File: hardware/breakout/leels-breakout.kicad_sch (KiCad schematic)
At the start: 18 parts, among them J2 Servo: 5V STEP DIR ENA GND, J3 Encoder: 5V GND A B Z, J4 5V in, J5 Nextion: 5V GND TX RX, J6 Shield GND, Q1 2N3904, U1 ESP32-C6-DevKitC-1, U2 74AHCT125

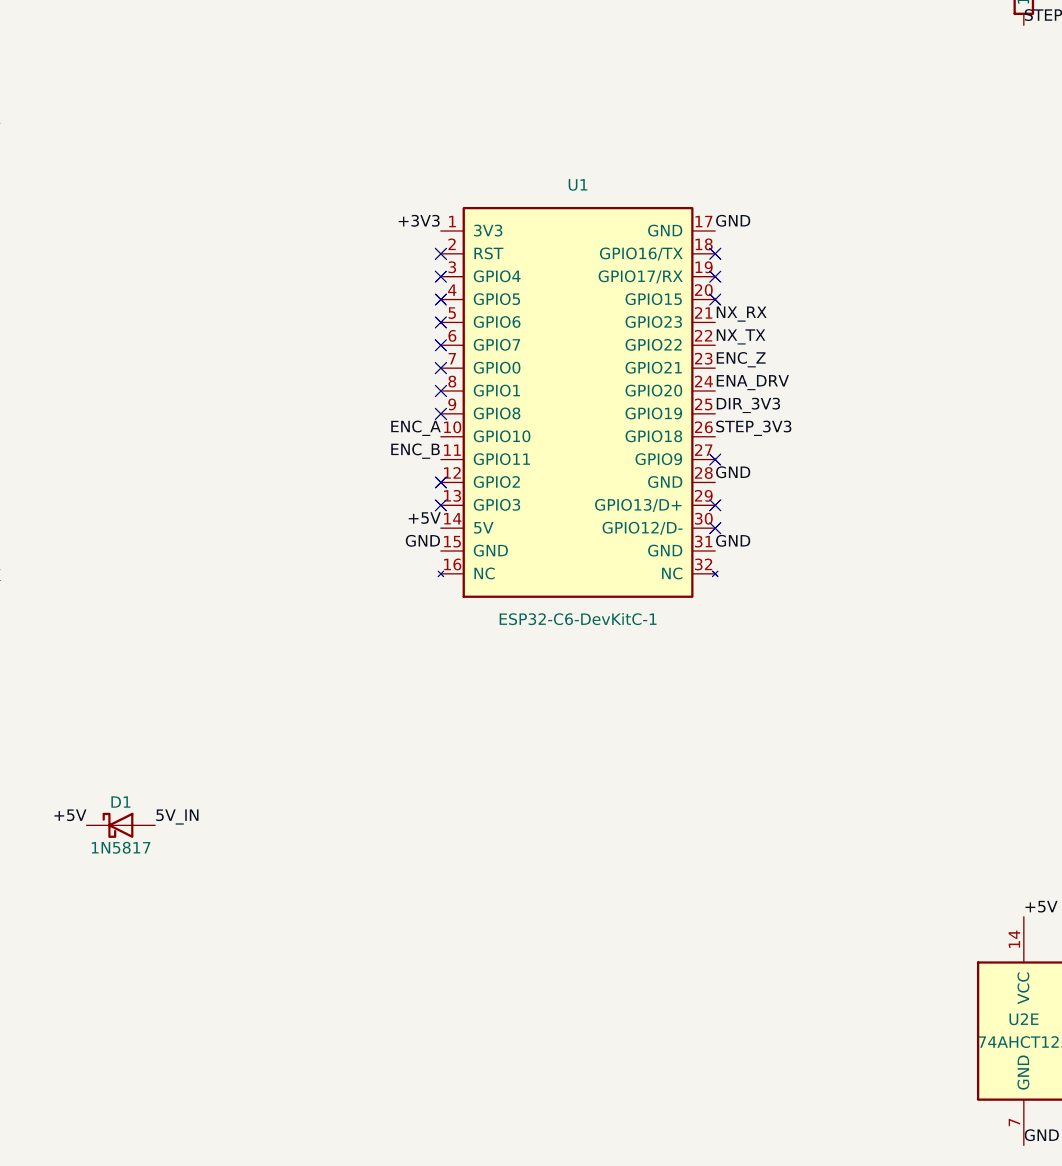
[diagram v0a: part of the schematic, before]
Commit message: Breakout: Espressif's DevKitC-1 symbol and footprint for U1
Use PCM_Espressif:ESP32-C6-DevKitC-1 (headers 22.86 mm apart, J3 pads
numbered 17-32 bottom to top) instead of the hand-made symbol, with the
nets reattached in Espressif's numbering and PWR_FLAGs on the rails.
ERC clean, no unconnected pins or orphan labels.

Co-Authored-By: Claude Opus 5.5 <noreply@anthropic.com>
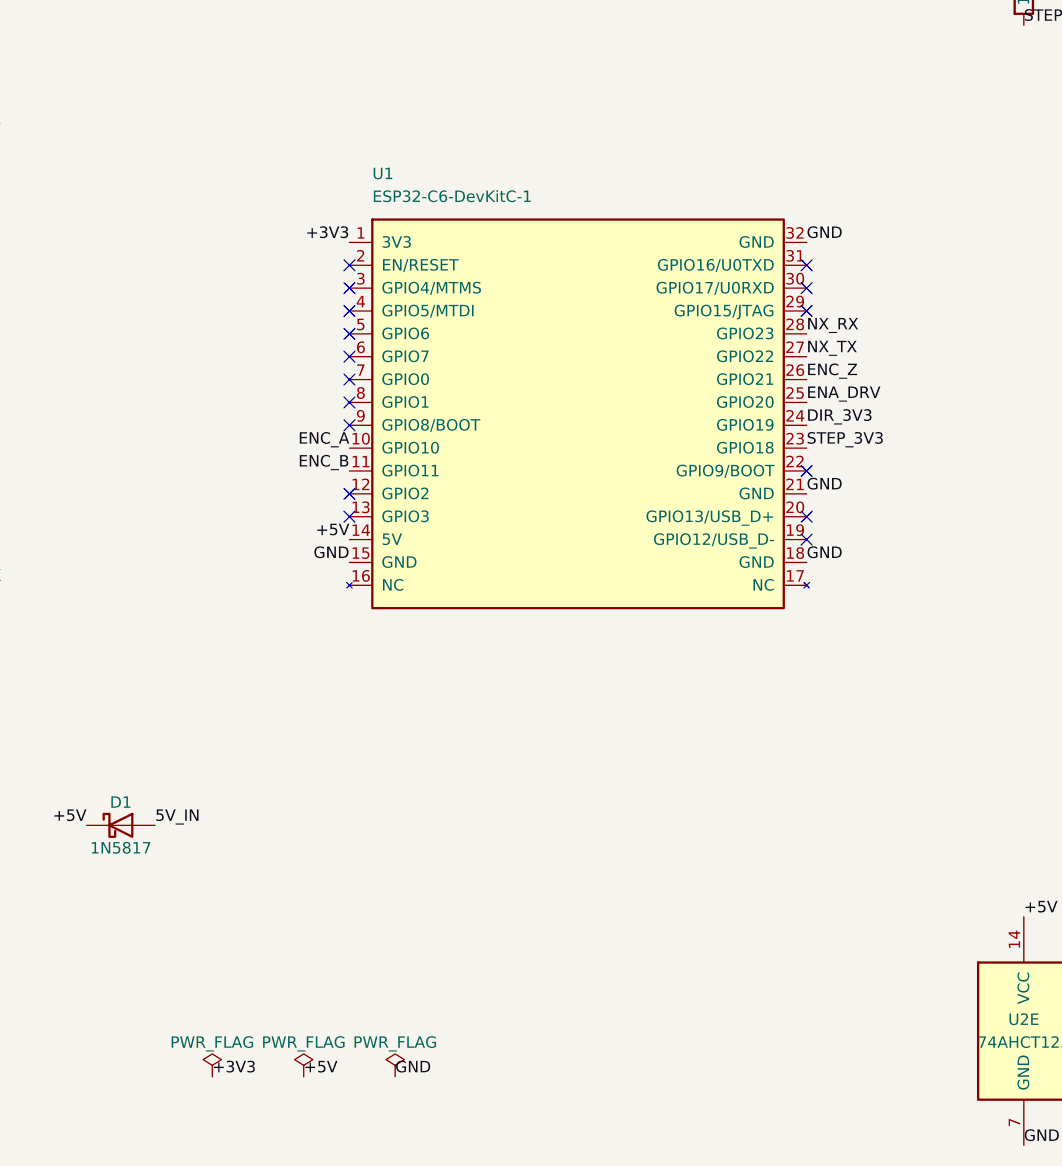
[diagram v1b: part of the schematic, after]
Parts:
- removed U1: ESP32-C6-DevKitC-1, symbol leels:ESP32-C6-DevKitC-1
- added U1: ESP32-C6-DevKitC-1, PCM_Espressif:ESP32-C6-DevKitC-1, symbol PCM_Espressif:ESP32-C6-DevKitC-1
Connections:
- net +3V3: now also U1.1 (3V3)
- net +5V: now also U1.14 (5V)
- net DIR_3V3: now also U1.24 (GPIO19)
- net ENA_DRV: now also U1.25 (GPIO20)
- net ENC_A: now also U1.10 (GPIO10)
- net ENC_B: now also U1.11 (GPIO11)
- net ENC_Z: now also U1.26 (GPIO21)
- net GND: now also U1.15 (GND), U1.18 (GND), U1.21 (GND), U1.32 (GND)
- net NX_RX: now also U1.28 (GPIO23)
- net NX_TX: now also U1.27 (GPIO22)
- net STEP_3V3: now also U1.23 (GPIO18)

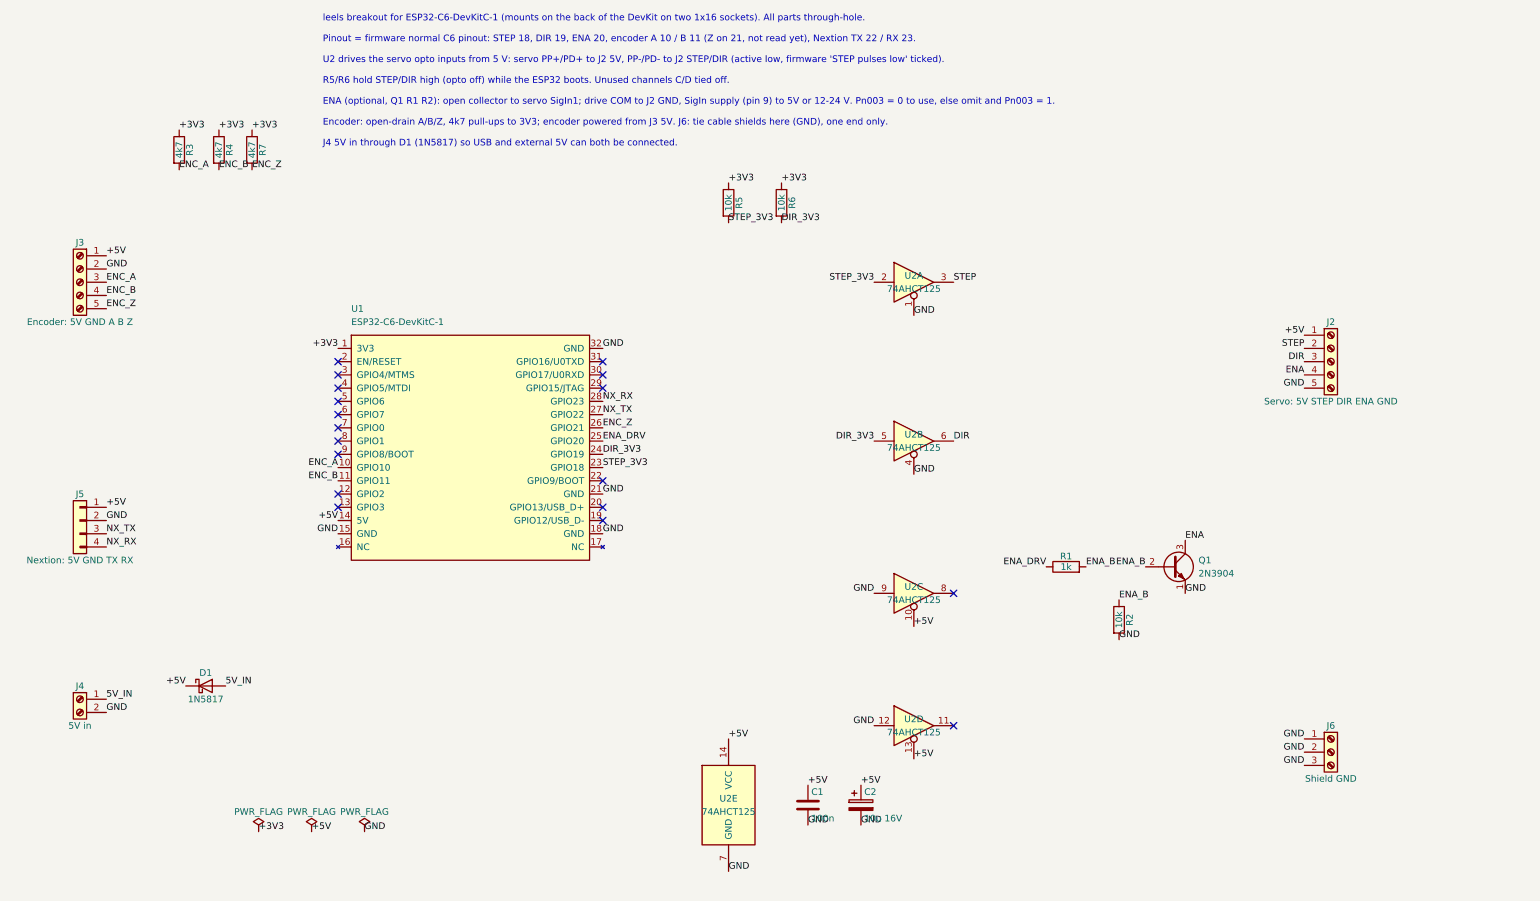
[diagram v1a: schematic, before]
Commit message: Breakout schematic: laid out by function, wired, labels only for ENC_Z
Encoder and power in on the left, the DevKit in the middle, the servo
chain (pull-ups, 74AHCT125, ENA transistor, terminal) and Nextion on the
right. Real wires and power symbols throughout; the only labels are the
ENC_Z global labels, which cross the sheet. PWR_FLAGs in their own block,
notes and title block. ERC clean, no orphans or unconnected pins.

Co-Authored-By: Claude Opus 5.5 <noreply@anthropic.com>
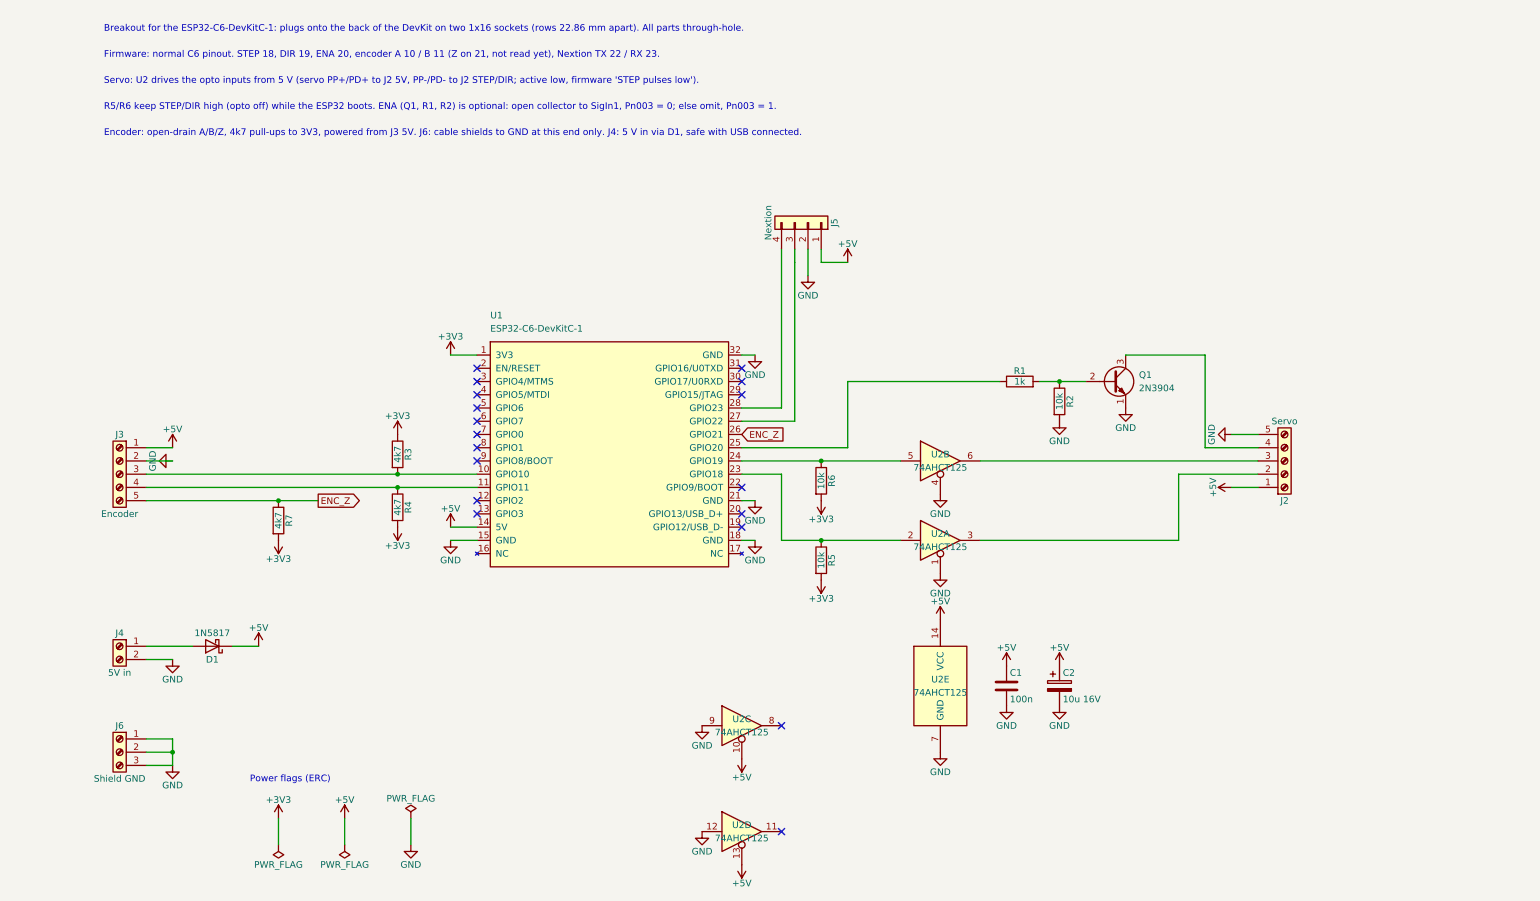
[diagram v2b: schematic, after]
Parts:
- J2: value Servo: 5V STEP DIR ENA GND -> Servo
- J3: value Encoder: 5V GND A B Z -> Encoder
- J5: value Nextion: 5V GND TX RX -> Nextion
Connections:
- net +3V3: now also R4.2, R5.2, R6.2, R7.2; no longer R4.1, R5.1, R6.1, R7.1
- net ENC_Z: now also R7.1; no longer R7.2
- net 5V_IN: no longer names the net of D1.2 (A), J4.1 (Pin_1)
- net DIR: no longer names the net of J2.3 (Pin_3), U2.6
- net DIR_3V3: no longer names the net of U1.24 (GPIO19), U2.5
- net DIR_3V3: now also R6.1; no longer R6.2
- net ENA: no longer names the net of J2.4 (Pin_4), Q1.3 (C)
- net ENA_B: no longer names the net of Q1.2 (B), R1.2, R2.1
- net ENA_DRV: no longer names the net of R1.1, U1.25 (GPIO20)
- net ENC_A: no longer names the net of J3.3 (Pin_3), R3.2, U1.10 (GPIO10)
- net ENC_B: no longer names the net of J3.4 (Pin_4), U1.11 (GPIO11)
- net ENC_B: now also R4.1; no longer R4.2
- net NX_RX: no longer names the net of J5.4 (Pin_4), U1.28 (GPIO23)
- net NX_TX: no longer names the net of J5.3 (Pin_3), U1.27 (GPIO22)
- net STEP: no longer names the net of J2.2 (Pin_2), U2.3
- net STEP_3V3: no longer names the net of U1.23 (GPIO18), U2.2
- net STEP_3V3: now also R5.1; no longer R5.2
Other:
- note added: "Breakout for the ESP32-C6-DevKitC-1: plugs onto the back of the DevKit on two 1x16 sockets (rows 22.86 mm apart). All parts through-hole."
- note added: "Encoder: open-drain A/B/Z, 4k7 pull-ups to 3V3, powered from J3 5V. J6: cable shields to GND at this end only. J4: 5 V in via D1, safe with USB connected."
- note added: "Firmware: normal C6 pinout. STEP 18, DIR 19, ENA 20, encoder A 10 / B 11 (Z on 21, not read yet), Nextion TX 22 / RX 23."
- note added: "Power flags (ERC)"
- note added: "R5/R6 keep STEP/DIR high (opto off) while the ESP32 boots. ENA (Q1, R1, R2) is optional: open collector to SigIn1, Pn003 = 0; else omit, Pn003 = 1."
- note added: "Servo: U2 drives the opto inputs from 5 V (servo PP+/PD+ to J2 5V, PP-/PD- to J2 STEP/DIR; active low, firmware 'STEP pulses low')."
- note removed: "ENA (optional, Q1 R1 R2): open collector to servo SigIn1; drive COM to J2 GND, SigIn supply (pin 9) to 5V or 12-24 V. Pn003 = 0 to use, else omit and Pn003 = 1."
- note removed: "Encoder: open-drain A/B/Z, 4k7 pull-ups to 3V3; encoder powered from J3 5V. J6: tie cable shields here (GND), one end only."
- note removed: "J4 5V in through D1 (1N5817) so USB and external 5V can both be connected."
- note removed: "Pinout = firmware normal C6 pinout: STEP 18, DIR 19, ENA 20, encoder A 10 / B 11 (Z on 21, not read yet), Nextion TX 22 / RX 23."
- note removed: "R5/R6 hold STEP/DIR high (opto off) while the ESP32 boots. Unused channels C/D tied off."
- note removed: "U2 drives the servo opto inputs from 5 V: servo PP+/PD+ to J2 5V, PP-/PD- to J2 STEP/DIR (active low, firmware 'STEP pulses low' ticked)."
- note removed: "leels breakout for ESP32-C6-DevKitC-1 (mounts on the back of the DevKit on two 1x16 sockets). All parts through-hole."
- title: (none) -> leels: ESP32-C6-DevKitC-1 breakout

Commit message: Breakout PCB: placement, routing and DRC-clean board
- build_pcb.py builds the board from the schematic netlist: outline (stops
  at the DevKit's PCB edge, nothing under the antenna), placement with
  the buffer and passives under the DevKit, terminals facing the edges,
  GND pours on both layers and stitching vias.
- route.py round-trips through Freerouting (Specctra DSN/SES); GND is
  left to the pours.
- leels.pretty: Espressif's DevKitC-1 footprint with the courtyard
  limited to the socket rows.
- Q1 on TO-92_Inline_Wide (the narrow one breaks 0.25 mm clearance).
- Net classes: 0.3 mm signals, 0.6 mm power and ground.
DRC: 0 violations, 0 unconnected, 0 schematic parity issues.

Co-Authored-By: Claude Opus 5.5 <noreply@anthropic.com>
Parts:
- Q1: footprint Package_TO_SOT_THT:TO-92_Inline -> Package_TO_SOT_THT:TO-92_Inline_Wide
- U1: footprint PCM_Espressif:ESP32-C6-DevKitC-1 -> leels:ESP32-C6-DevKitC-1_Sockets
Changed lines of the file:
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@@
 			)
 		)
-		(property "Footprint" "PCM_Espressif:ESP32-C6-DevKitC-1"
+		(property "Footprint" "leels:ESP32-C6-DevKitC-1_Sockets"
 			(at 127 101.6 0)
 			(hide yes)
@@
 			)
 		)
-		(property "Footprint" "Package_TO_SOT_THT:TO-92_Inline"
+		(property "Footprint" "Package_TO_SOT_THT:TO-92_Inline_Wide"
 			(at 223.52 88.9 0)
 			(hide yes)

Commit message: Breakout rev A: encoder RC filters, Nextion before D1, Dupont header, holes
- Encoder A/B/Z: 220R series at the terminal, 220p to GND at the GPIO
  (with the existing 4k7 pull-up), for noise and ESD.
- Nextion power (J5, new J7) on 5V_IN ahead of D1: no Schottky drop for
  the display; it needs J4 power.
- J7: 1x4 2.54 mm header in parallel with the JST for Dupont plugs.
- C1 axial (laid flat) right at U2's supply pin; Q1 laid flat
  (TO-92 staggered horizontal, clearance-safe).
- Three M3 mounting holes; board 51 x 70.1 mm.
DRC: 1 warning (U2 pin 12 thermal on F.Cu, connected via B.Cu), 0
unconnected, 0 parity issues; ERC clean.

Co-Authored-By: Claude Opus 5.5 <noreply@anthropic.com>
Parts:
- added C3, C4, C5: 220p, Capacitor_THT:C_Axial_L3.8mm_D2.6mm_P7.50mm_Horizontal, symbol Device:C
- added J7: Nextion (Dupont), Connector_PinHeader_2.54mm:PinHeader_1x04_P2.54mm_Vertical, symbol Connector_Generic:Conn_01x04
- added R10, R8, R9: 220, Resistor_THT:R_Axial_DIN0207_L6.3mm_D2.5mm_P7.62mm_Horizontal, symbol Device:R
- C1: footprint Capacitor_THT:C_Disc_D5.0mm_W2.5mm_P5.00mm -> Capacitor_THT:C_Axial_L3.8mm_D2.6mm_P7.50mm_Horizontal
- Q1: footprint Package_TO_SOT_THT:TO-92_Inline_Wide -> Package_TO_SOT_THT:TO-92_W4.0mm_StaggerEven_Horizontal_FlatSideDown
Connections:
- net +5V: no longer J5.1 (Pin_1)
- net ENC_Z: now also C5.1, R10.2; no longer J3.5 (Pin_5)
- net GND: now also C3.1, C4.2, C5.2, J7.2 (Pin_2)
- net at R3.2, U1.10 (GPIO10): now also C3.2, R8.2; no longer J3.3 (Pin_3)
- net at R4.1, U1.11 (GPIO11): now also C4.1, R9.2; no longer J3.4 (Pin_4)
- net 5V_IN: now reaches D1.2 (A), J4.1 (Pin_1)
- net 5V_IN: now also J5.1 (Pin_1), J7.1 (Pin_1)
- net NX_TX: now reaches J5.3 (Pin_3), U1.27 (GPIO22)
- net NX_TX: now also J7.3 (Pin_3)
- net NX_RX: now reaches J5.4 (Pin_4), U1.28 (GPIO23)
- net NX_RX: now also J7.4 (Pin_4)
- new net: J3.5 (Pin_5), R10.1
- new net: J3.4 (Pin_4), R9.1
- new net: J3.3 (Pin_3), R8.1
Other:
- note added: "Encoder: open-drain A/B/Z, 220R series + 4k7 pull-up to 3V3 + 220p to GND each, powered from J3 5V. J6: cable shields to GND at this end only. J4: 5 V in via D1. Nextion (J5/J7) takes 5V_IN ahead of D1, so it needs J4 power."
- note removed: "Encoder: open-drain A/B/Z, 4k7 pull-ups to 3V3, powered from J3 5V. J6: cable shields to GND at this end only. J4: 5 V in via D1, safe with USB connected."
